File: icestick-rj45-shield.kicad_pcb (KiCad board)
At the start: 2 copper layers, 21 parts, among them J1 Conn_01x10, J3 Conn_01x10, U1 Si8640BB-B-IS1, U2 Si8640BB-B-IS1, U3 Si8640BB-B-IS1, U4 Si8640BB-B-IS1

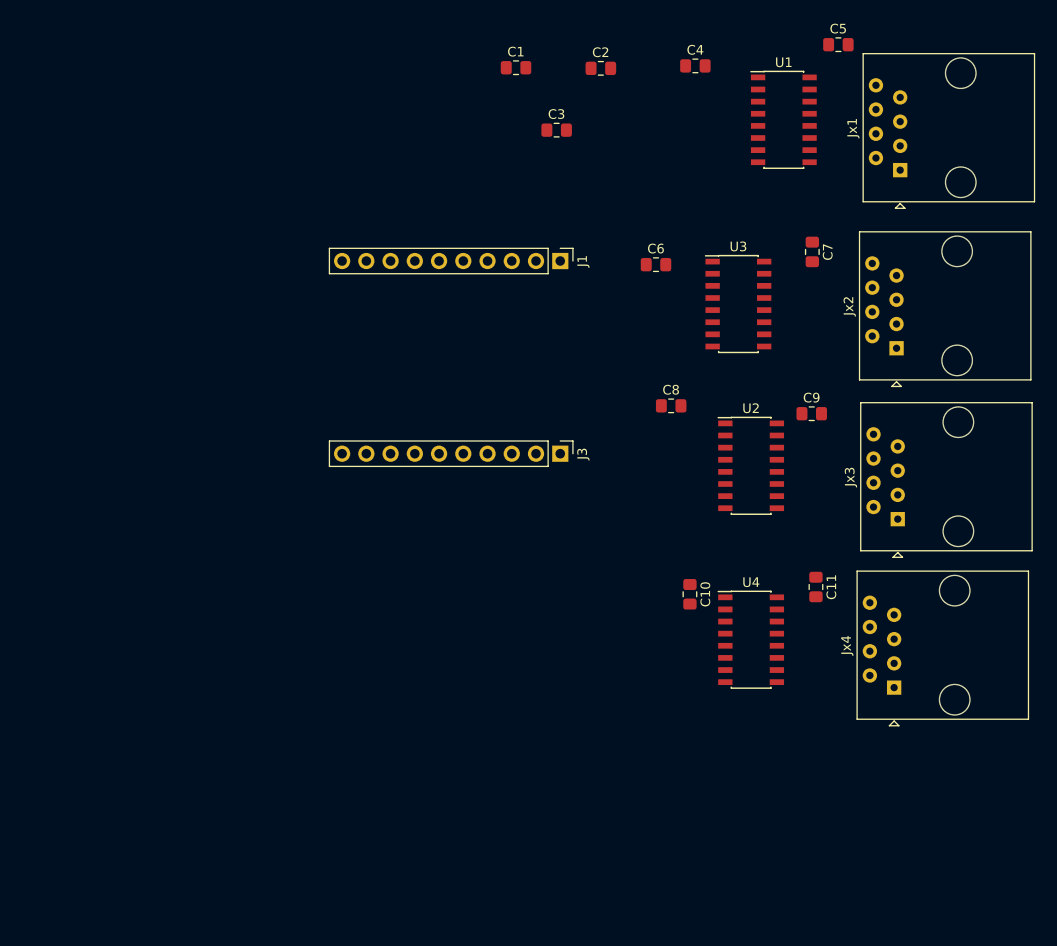
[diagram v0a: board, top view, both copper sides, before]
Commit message: Continued layouting
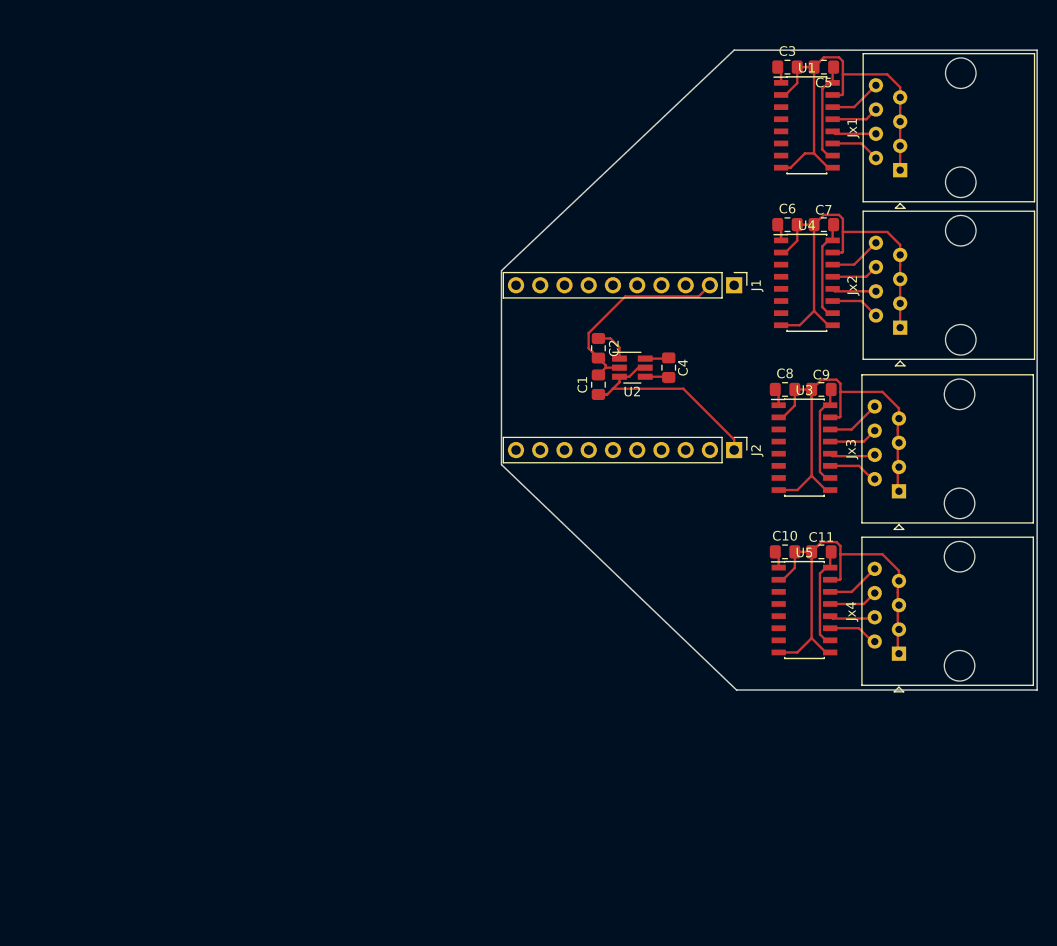
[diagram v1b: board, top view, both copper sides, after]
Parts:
- removed J3: Conn_01x10, Connector_PinHeader_2.54mm:PinHeader_1x10_P2.54mm_Vertical
- added J2: Conn_01x10, Connector_PinHeader_2.54mm:PinHeader_1x10_P2.54mm_Vertical, F.Cu at (183.4, 94.2)
- added U5: Si8640BB-B-IS1, Package_SO:SOIC-16_3.9x9.9mm_P1.27mm, F.Cu at (190.8, 111.0)
- C1, C2: value 2.2uF -> 220nF
- U2: value Si8640BB-B-IS1 -> REG71050; footprint Package_SO:SOIC-16_3.9x9.9mm_P1.27mm -> Package_TO_SOT_SMD:SOT-23-6_Handsoldering
- moved U4 37.9 mm to (191.0, 76.7)
- moved C1 34.3 mm to (169.2, 87.4), turned to 90 degrees
- moved C4 31.7 mm to (176.5, 85.6), turned to 90 degrees
- moved C2 29.3 mm to (169.2, 83.6), turned to 270 degrees
- moved C3 25.1 mm to (189.0, 54.1)
- moved J1 18.4 mm to (183.4, 77.0)
- moved U3 16.6 mm to (190.8, 94.0)
- moved U2 16.1 mm to (172.7, 85.6)
- moved C6 14.4 mm to (189.0, 70.6)
- moved C8 12.1 mm to (188.7, 87.9)
- moved C10 10.9 mm to (188.7, 104.9), turned to 0 degrees
- moved C11 3.73 mm to (192.5, 104.9), turned to 180 degrees
- moved Jx4 3.59 mm to (200.7, 115.6)
- moved C7 3.10 mm to (192.8, 70.6), turned to 180 degrees
- moved Jx3 2.92 mm to (200.7, 98.6)
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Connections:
- C3 pad 1: Net-(C3-Pad1) -> +3V3
- C3 pad 2: Net-(C3-Pad2) -> GND
- C4 pad 1: +3V3 -> Net-(C4-Pad1)
- C4 pad 2: GND -> Net-(C4-Pad2)
- U1 pad 3: /iCEstick connector/FPGA_112 -> /iCEstick connector/FPGA_116
- U1 pad 4: /iCEstick connector/FPGA_113 -> /iCEstick connector/FPGA_117
- U1 pad 5: /iCEstick connector/FPGA_114 -> /iCEstick connector/FPGA_118
- U1 pad 6: /iCEstick connector/FPGA_115 -> /iCEstick connector/FPGA_119
- U2 pad 1: +3V3 -> +5V
- U2 pad 3: /iCEstick connector/FPGA_62 -> +3V3
- U2 pad 4: /iCEstick connector/FPGA_61 -> Net-(C4-Pad1)
- U2 pad 5: /iCEstick connector/FPGA_60 -> +3V3
- U2 pad 6: /iCEstick connector/FPGA_56 -> Net-(C4-Pad2)
- U3 pad 11: /Connector 2/OUT4 -> /Connector 3/OUT4
- U3 pad 12: /Connector 2/OUT3 -> /Connector 3/OUT3
- U3 pad 13: /Connector 2/OUT2 -> /Connector 3/OUT2
- U3 pad 14: /Connector 2/OUT1 -> /Connector 3/OUT1
- U3 pad 3: /iCEstick connector/FPGA_116 -> /iCEstick connector/FPGA_62
- U3 pad 4: /iCEstick connector/FPGA_117 -> /iCEstick connector/FPGA_61
- U3 pad 5: /iCEstick connector/FPGA_118 -> /iCEstick connector/FPGA_60
- U3 pad 6: /iCEstick connector/FPGA_119 -> /iCEstick connector/FPGA_56
- U4 pad 11: /Connector 4/OUT4 -> /Connector 2/OUT4
- U4 pad 12: /Connector 4/OUT3 -> /Connector 2/OUT3
- U4 pad 13: /Connector 4/OUT2 -> /Connector 2/OUT2
- U4 pad 14: /Connector 4/OUT1 -> /Connector 2/OUT1
- U4 pad 3: /iCEstick connector/FPGA_48 -> /iCEstick connector/FPGA_112
- U4 pad 4: /iCEstick connector/FPGA_47 -> /iCEstick connector/FPGA_113
- U4 pad 5: /iCEstick connector/FPGA_45 -> /iCEstick connector/FPGA_114
- U4 pad 6: /iCEstick connector/FPGA_44 -> /iCEstick connector/FPGA_115
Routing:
- net GND: track 0.00 -> 201.3 mm
- net +5V: track 0.00 -> 46.7 mm
- net +3V3: track 0.00 -> 29.6 mm
- net /Connector 2/OUT1: track 0.00 -> 5.49 mm
- net /Connector 1/OUT1: track 0.00 -> 5.49 mm
- net /Connector 4/OUT1: track 0.00 -> 5.49 mm
- net /Connector 3/OUT1: track 0.00 -> 5.49 mm
- net /Connector 2/OUT4: track 0.00 -> 5.17 mm
- net /Connector 1/OUT4: track 0.00 -> 5.17 mm
- net /Connector 4/OUT4: track 0.00 -> 5.17 mm
- net /Connector 3/OUT4: track 0.00 -> 5.17 mm
- net /Connector 1/OUT2: track 0.00 -> 4.96 mm
- net /Connector 2/OUT2: track 0.00 -> 4.96 mm
- net /Connector 4/OUT2: track 0.00 -> 4.96 mm
- net /Connector 3/OUT2: track 0.00 -> 4.96 mm
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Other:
- board outline added: 56.1 x 67.1 mm

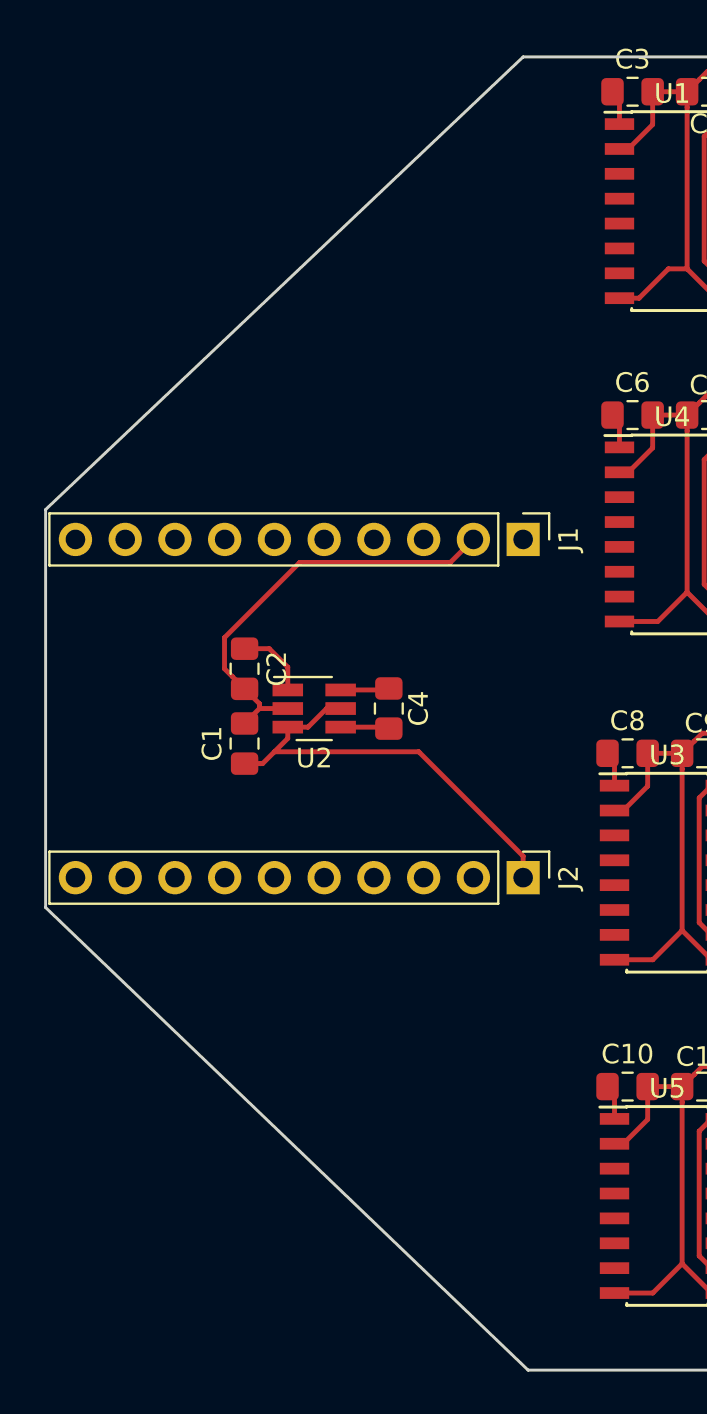
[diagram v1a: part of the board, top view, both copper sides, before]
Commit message: Fixed iCEstick header distance
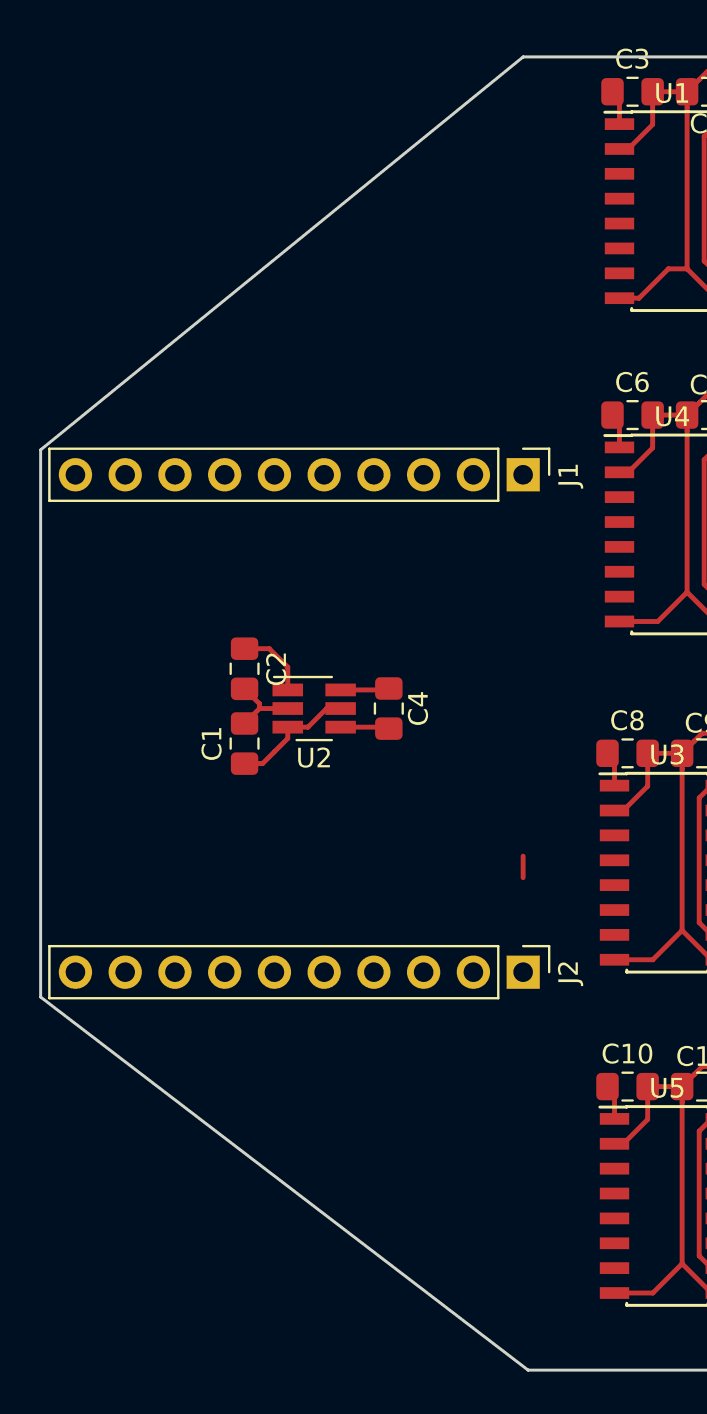
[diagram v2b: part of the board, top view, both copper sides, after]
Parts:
- moved J2 4.83 mm to (183.4, 99.1)
- moved J1 3.30 mm to (183.4, 73.7)
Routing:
- net GND: track 201.3 -> 183.4 mm
- net +3V3: track 29.6 -> 14.7 mm
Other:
- board size 56.1 x 67.1 mm -> 56.4 x 67.1 mm

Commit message: Routed all the signals
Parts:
- turned C3 to 180 degrees
- turned C6 to 180 degrees
- turned C8 to 180 degrees
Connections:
- U1 pad 3: /iCEstick connector/FPGA_116 -> /iCEstick connector/FPGA_119
- U1 pad 4: /iCEstick connector/FPGA_117 -> /iCEstick connector/FPGA_118
- U1 pad 5: /iCEstick connector/FPGA_118 -> /iCEstick connector/FPGA_117
- U1 pad 6: /iCEstick connector/FPGA_119 -> /iCEstick connector/FPGA_116
- U1 pad 7: Net-(U1-Pad7) -> (no net)
- U3 pad 3: /iCEstick connector/FPGA_62 -> /iCEstick connector/FPGA_56
- U3 pad 4: /iCEstick connector/FPGA_61 -> /iCEstick connector/FPGA_60
- U3 pad 5: /iCEstick connector/FPGA_60 -> /iCEstick connector/FPGA_61
- U3 pad 6: /iCEstick connector/FPGA_56 -> /iCEstick connector/FPGA_62
- U3 pad 7: Net-(U3-Pad7) -> (no net)
- U4 pad 7: Net-(U4-Pad7) -> (no net)
- U5 pad 7: Net-(U5-Pad7) -> (no net)
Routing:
- net GND: track 183.4 -> 57.7 mm, vias 0 -> 14
- net +3V3: track 14.7 -> 122.9 mm
- net +5V: track 46.7 -> 97.8 mm
- net /iCEstick connector/FPGA_119: track 0.00 -> 34.1 mm
- net /iCEstick connector/FPGA_44: track 0.00 -> 33.3 mm
- net /iCEstick connector/FPGA_118: track 0.00 -> 31.1 mm
- net /iCEstick connector/FPGA_45: track 0.00 -> 30.2 mm
- net /iCEstick connector/FPGA_117: track 0.00 -> 28.0 mm
- net /iCEstick connector/FPGA_47: track 0.00 -> 27.1 mm
- net /iCEstick connector/FPGA_116: track 0.00 -> 24.9 mm
- net /iCEstick connector/FPGA_48: track 0.00 -> 24.1 mm
- net /iCEstick connector/FPGA_56: track 0.00 -> 20.3 mm
- net /iCEstick connector/FPGA_115: track 0.00 -> 19.7 mm
- net /iCEstick connector/FPGA_60: track 0.00 -> 17.2 mm
- net /iCEstick connector/FPGA_114: track 0.00 -> 16.6 mm
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- added copper zone on B.Cu, net GND
- added copper zone on F.Cu, net GND

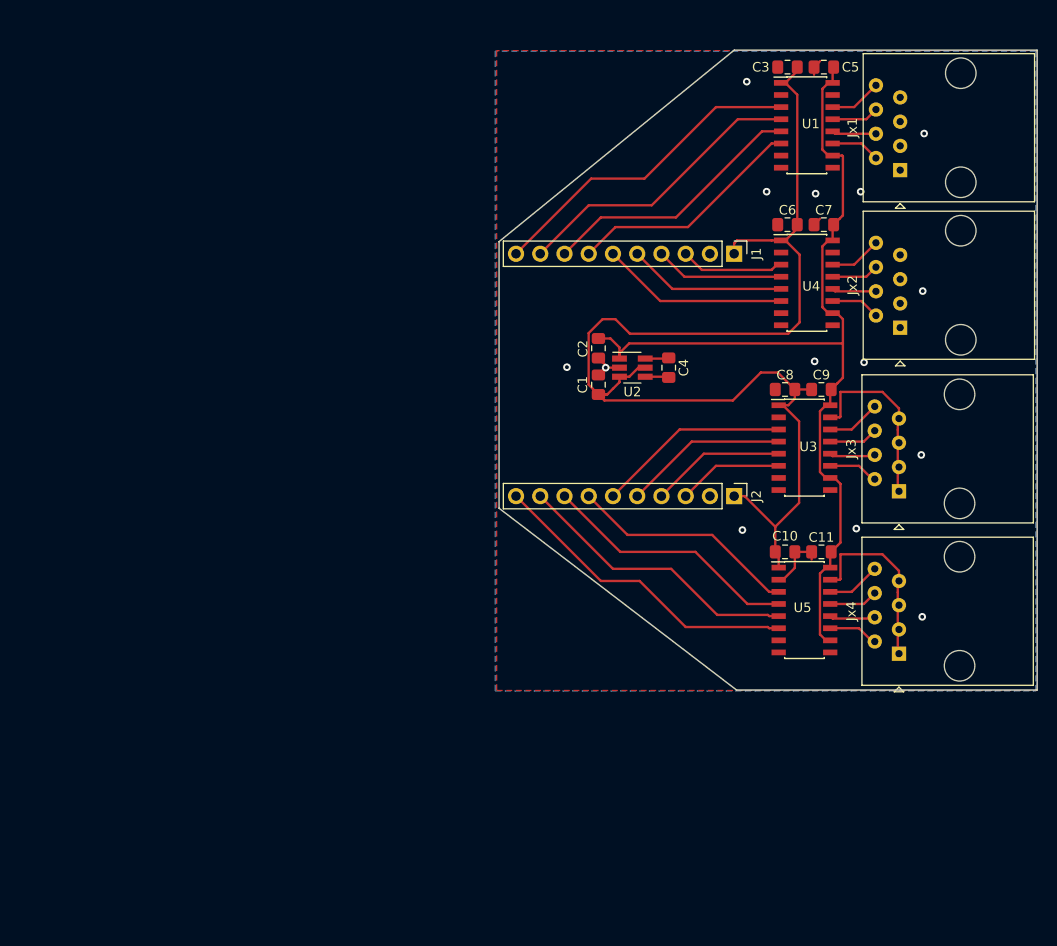
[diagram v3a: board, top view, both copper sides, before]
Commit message: PCB: Added a couple of GND vias
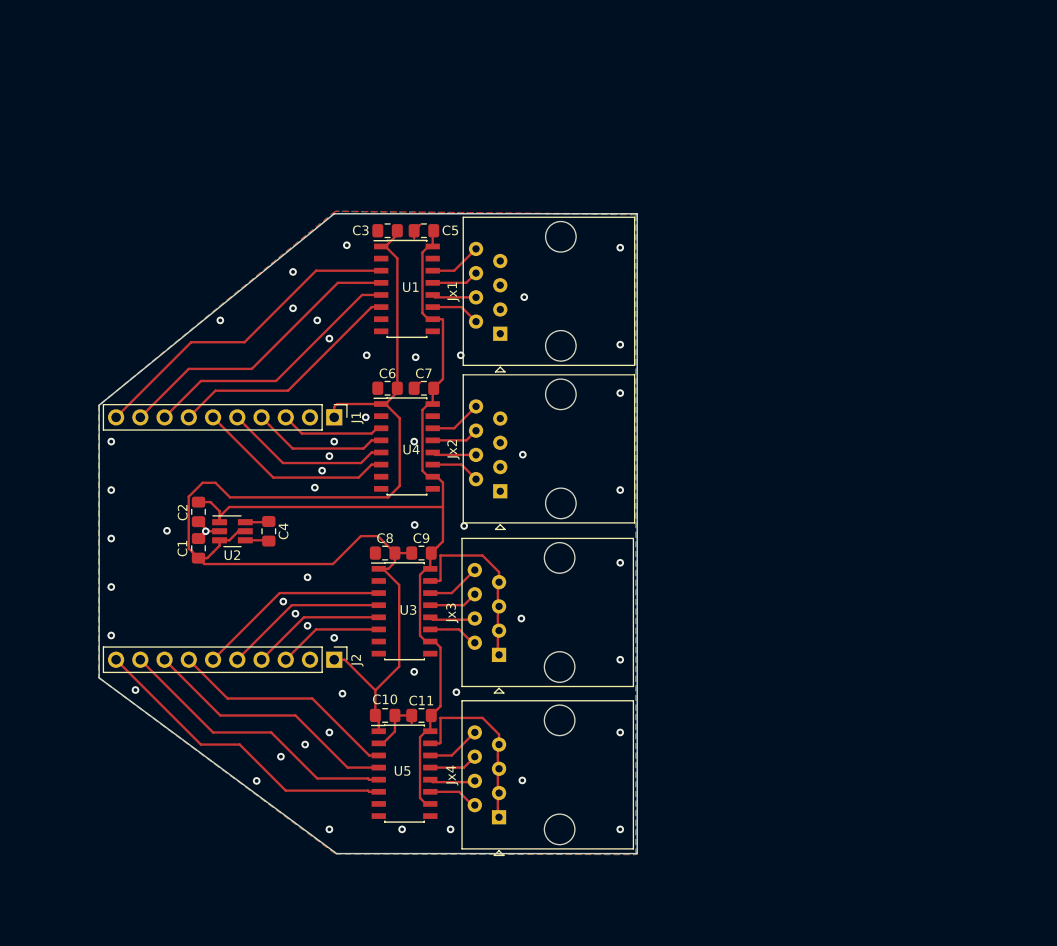
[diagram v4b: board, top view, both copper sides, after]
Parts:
- moved C3 45.3 mm to (147.1, 71.2)
- moved C5 45.3 mm to (150.9, 71.2)
- moved C6 45.3 mm to (147.1, 87.8)
- moved C7 45.3 mm to (150.9, 87.8)
- moved J1 45.3 mm to (141.5, 90.8)
- moved Jx2 45.3 mm to (158.9, 98.6)
- moved Jx4 45.3 mm to (158.8, 132.7)
- moved U1 45.3 mm to (149.1, 77.3)
- moved C10 45.3 mm to (146.8, 122.0)
- moved C11 45.3 mm to (150.6, 122.0)
- moved C4 45.3 mm to (134.6, 102.7)
- moved C8 45.3 mm to (146.8, 105.0)
- moved C9 45.3 mm to (150.6, 105.0)
- moved J2 45.3 mm to (141.5, 116.2)
- moved Jx1 45.3 mm to (158.9, 82.0)
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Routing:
- net /iCEstick connector/FPGA_115: track 19.7 -> 20.8 mm
- net /iCEstick connector/FPGA_114: track 16.6 -> 17.5 mm
- net /iCEstick connector/FPGA_113: track 13.5 -> 14.2 mm
- net GND: vias 14 -> 52
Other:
- outline, holes or cut-outs redrawn
